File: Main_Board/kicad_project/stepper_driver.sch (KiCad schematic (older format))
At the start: 13 parts

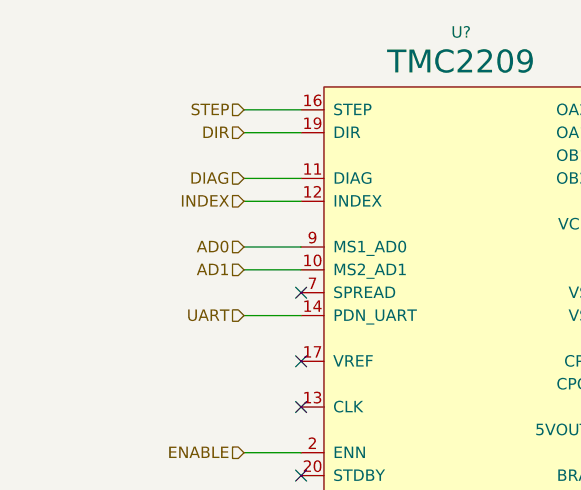
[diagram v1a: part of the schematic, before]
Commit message: add readmes, add MCU to main board, update footprints on interface board
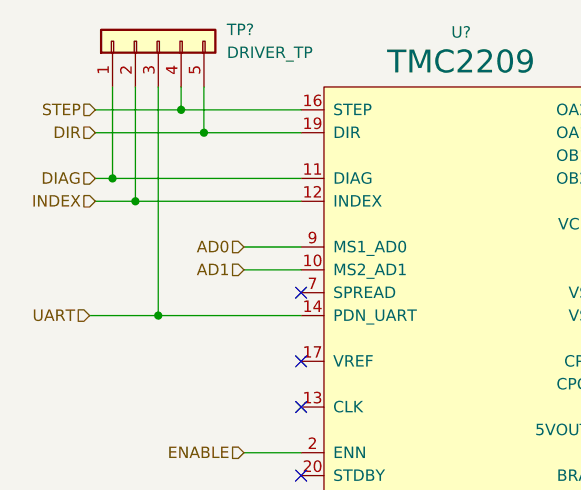
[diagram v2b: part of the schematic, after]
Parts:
- added TP?: DRIVER_TP, Connector_PinHeader_2.54mm:PinHeader_1x05_P2.54mm_Vertical, symbol Connector_Generic:Conn_01x05
- J?: footprint Connector_PinHeader_2.54mm:PinHeader_1x04_P2.54mm_Vertical -> Connector_PinHeader_2.54mm:PinHeader_1x04_P2.54mm_Horizontal
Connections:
- net DIAG: now also TP?.1 (Pin_1)
- net DIR: now also TP?.5 (Pin_5)
- net INDEX: now also TP?.2 (Pin_2)
- net STEP: now also TP?.4 (Pin_4)
- net UART: now also TP?.3 (Pin_3)
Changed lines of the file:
@@
 EESchema Schematic File Version 4
-LIBS:main_board-cache
-EELAYER 29 0
+EELAYER 30 0
 EELAYER END
 $Descr A4 11693 8268
 encoding utf-8
-Sheet 2 6
+Sheet 2 7
 Title ""
 Date ""
@@
 Text HLabel 4100 2950 0    50   Input ~ 0
 AD1
-Text HLabel 4100 3150 0    50   Input ~ 0
+Text HLabel 3425 3150 0    50   Input ~ 0
 UART
-Text HLabel 4100 2650 0    50   Input ~ 0
+Text HLabel 3450 2650 0    50   Input ~ 0
 INDEX
-Text HLabel 4100 2550 0    50   Input ~ 0
+Text HLabel 3450 2550 0    50   Input ~ 0
 DIAG
-Text HLabel 4100 2350 0    50   Input ~ 0
+Text HLabel 3450 2350 0    50   Input ~ 0
 DIR
-Text HLabel 4100 2250 0    50   Input ~ 0
+Text HLabel 3450 2250 0    50   Input ~ 0
 STEP
 Wire Wire Line
-	4350 2250 4100 2250
-Wire Wire Line
-	4100 2350 4350 2350
-Wire Wire Line
-	4350 2550 4100 2550
-Wire Wire Line
-	4100 2650 4350 2650
-Wire Wire Line
 	4350 2850 4100 2850
 Wire Wire Line
 	4100 2950 4350 2950
-Wire Wire Line
-	4350 3150 4100 3150
 Wire Wire Line
 	4350 3750 4100 3750
@@
 F 0 "J?" H 6405 2342 50  0000 L CNN
 F 1 "MOTOR" H 6405 2251 50  0000 L CNN
-F 2 "Connector_PinHeader_2.54mm:PinHeader_1x04_P2.54mm_Vertical" H 6325 2350 50  0001 C CNN
+F 2 "Connector_PinHeader_2.54mm:PinHeader_1x04_P2.54mm_Horizontal" H 6325 2350 50  0001 C CNN
 F 3 "~" H 6325 2350 50  0001 C CNN
 	1    6325 2350
@@
 Wire Wire Line
 	7550 3050 7600 3050
+$Comp
+L Connector_Generic:Conn_01x05 TP?
+U 1 1 5F51F4C4
+P 3725 1950
+F 0 "TP?" V 3775 1650 50  0000 R CNN
+F 1 "DRIVER_TP" V 3675 1650 50  0000 R CNN
+F 2 "Connector_PinHeader_2.54mm:PinHeader_1x05_P2.54mm_Vertical" H 3725 1950 50  0001 C CNN
+F 3 "~" H 3725 1950 50  0001 C CNN
+	1    3725 1950
+	0    -1   -1   0
+$EndComp
+Wire Wire Line
+	3450 2350 3925 2350
+Wire Wire Line
+	3450 2250 3825 2250
+Wire Wire Line
+	3450 2550 3525 2550
+Wire Wire Line
+	3450 2650 3625 2650
+Wire Wire Line
+	3425 3150 3725 3150
+Wire Wire Line
+	3525 2150 3525 2550
+Connection ~ 3525 2550
+Wire Wire Line
+	3525 2550 4350 2550
+Wire Wire Line
+	3625 2150 3625 2650
+Connection ~ 3625 2650
+Wire Wire Line
+	3625 2650 4350 2650
+Wire Wire Line
+	3725 2150 3725 3150
+Connection ~ 3725 3150
+Wire Wire Line
+	3725 3150 4350 3150
+Wire Wire Line
+	3825 2150 3825 2250
+Connection ~ 3825 2250
+Wire Wire Line
+	3825 2250 4350 2250
+Wire Wire Line
+	3925 2150 3925 2350
+Connection ~ 3925 2350
+Wire Wire Line
+	3925 2350 4350 2350
 $EndSCHEMATC

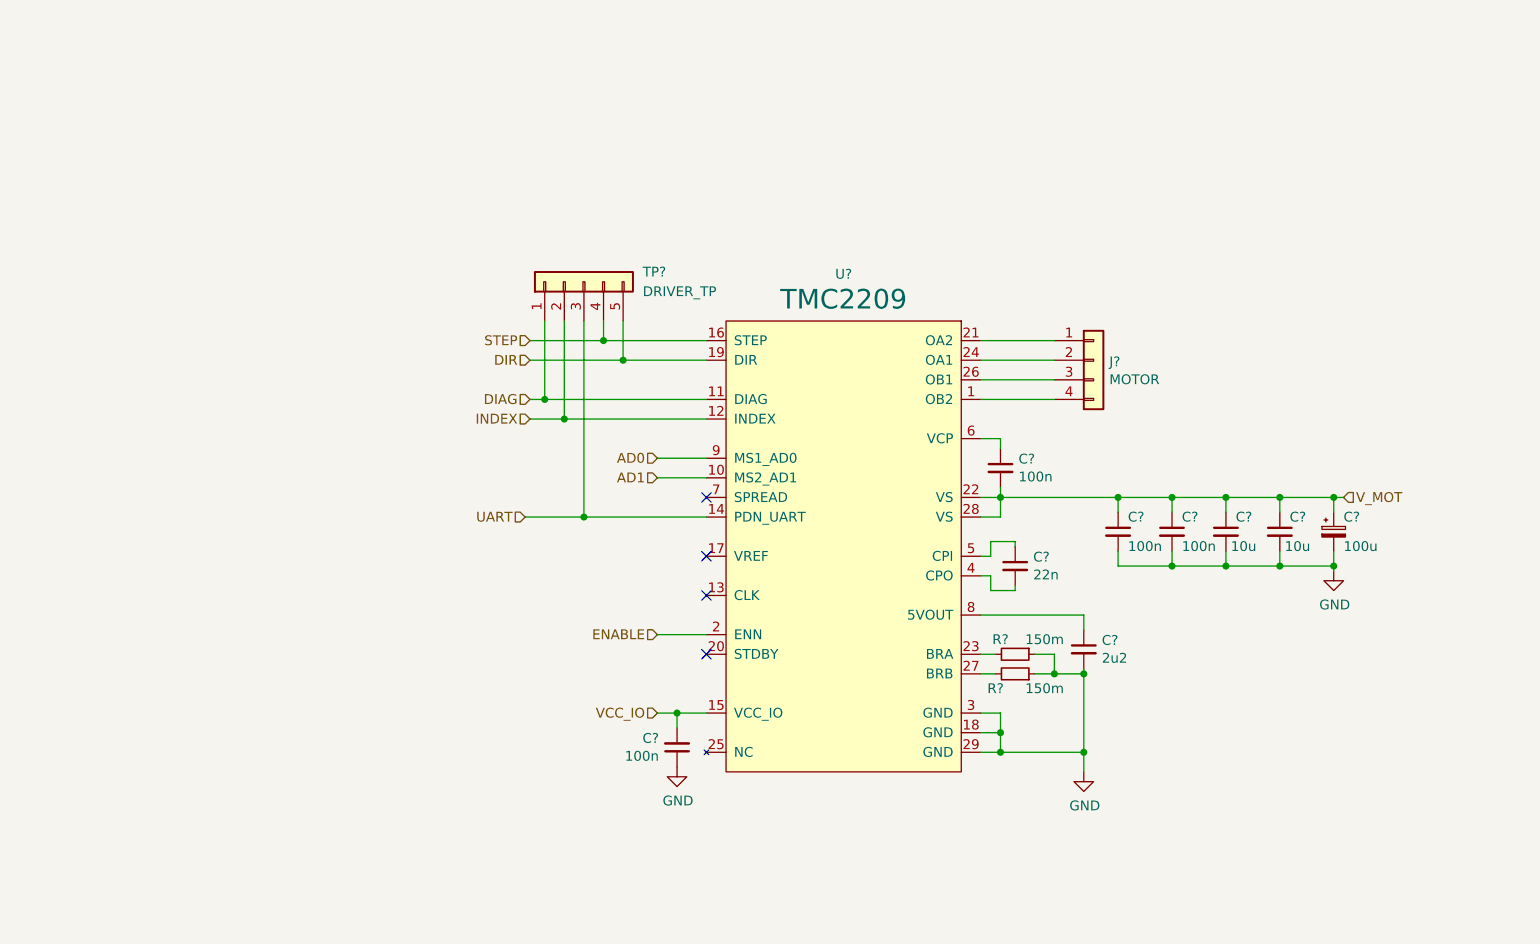
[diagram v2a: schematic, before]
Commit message: add input/output schematic, add documentation
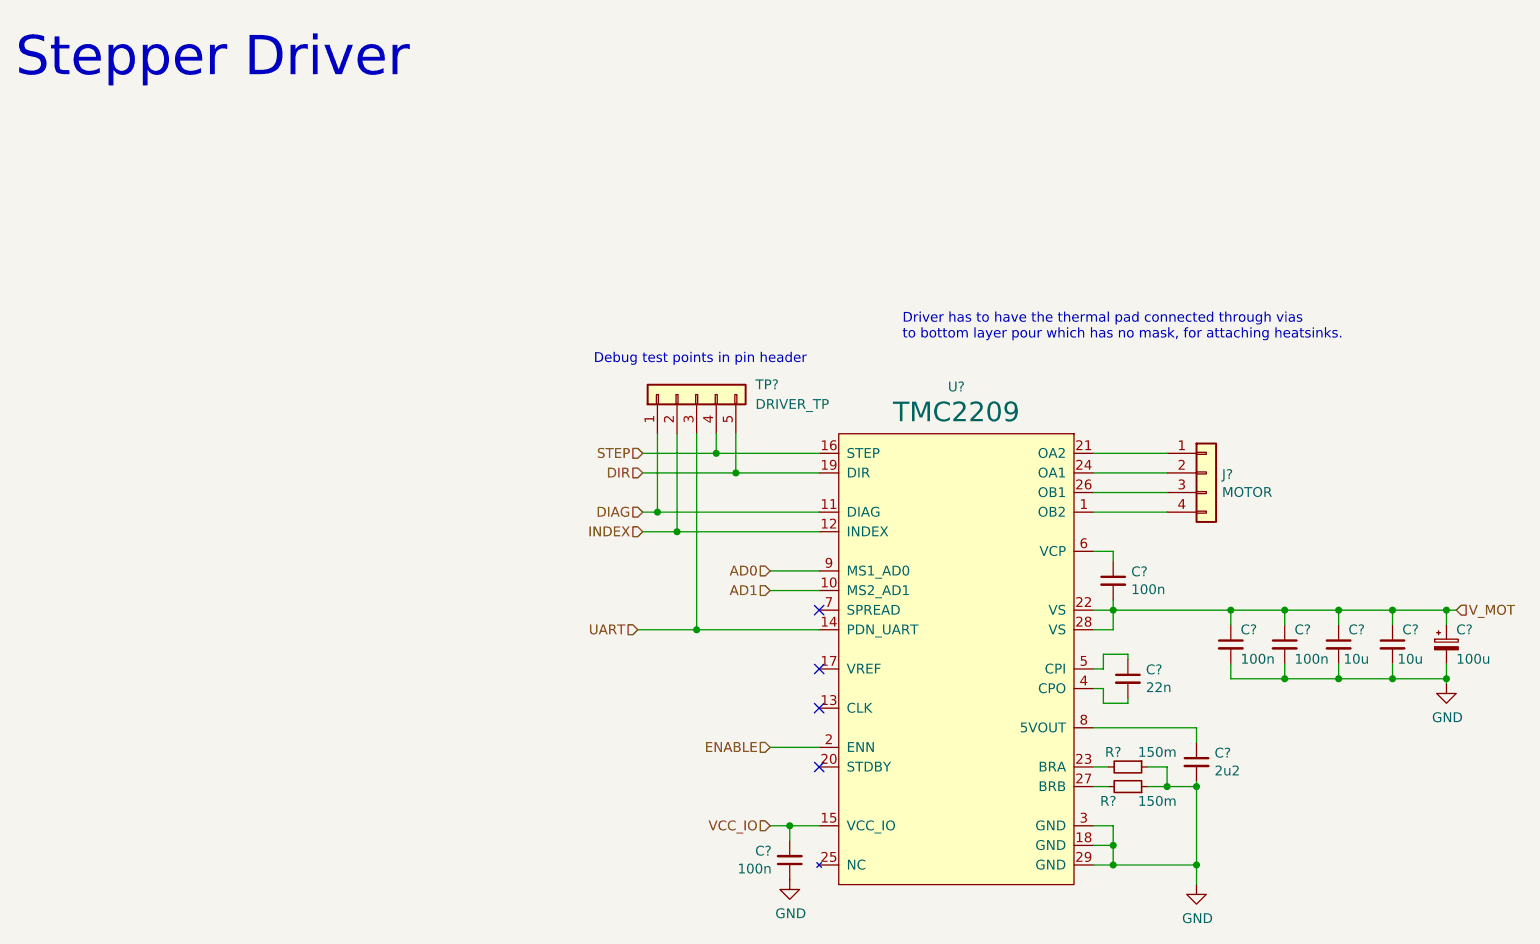
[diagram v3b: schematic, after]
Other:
- note added: "Debug test points in pin header"
- note added: "Driver has to have the thermal pad connected through vias\nto bottom layer pour which has no mask, for attaching heatsinks."
- note added: "Stepper Driver"
- moved on the sheet: C?, J?, R?, TP?, U?

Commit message: progress?
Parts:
- gave numbers to parts that had none: 14

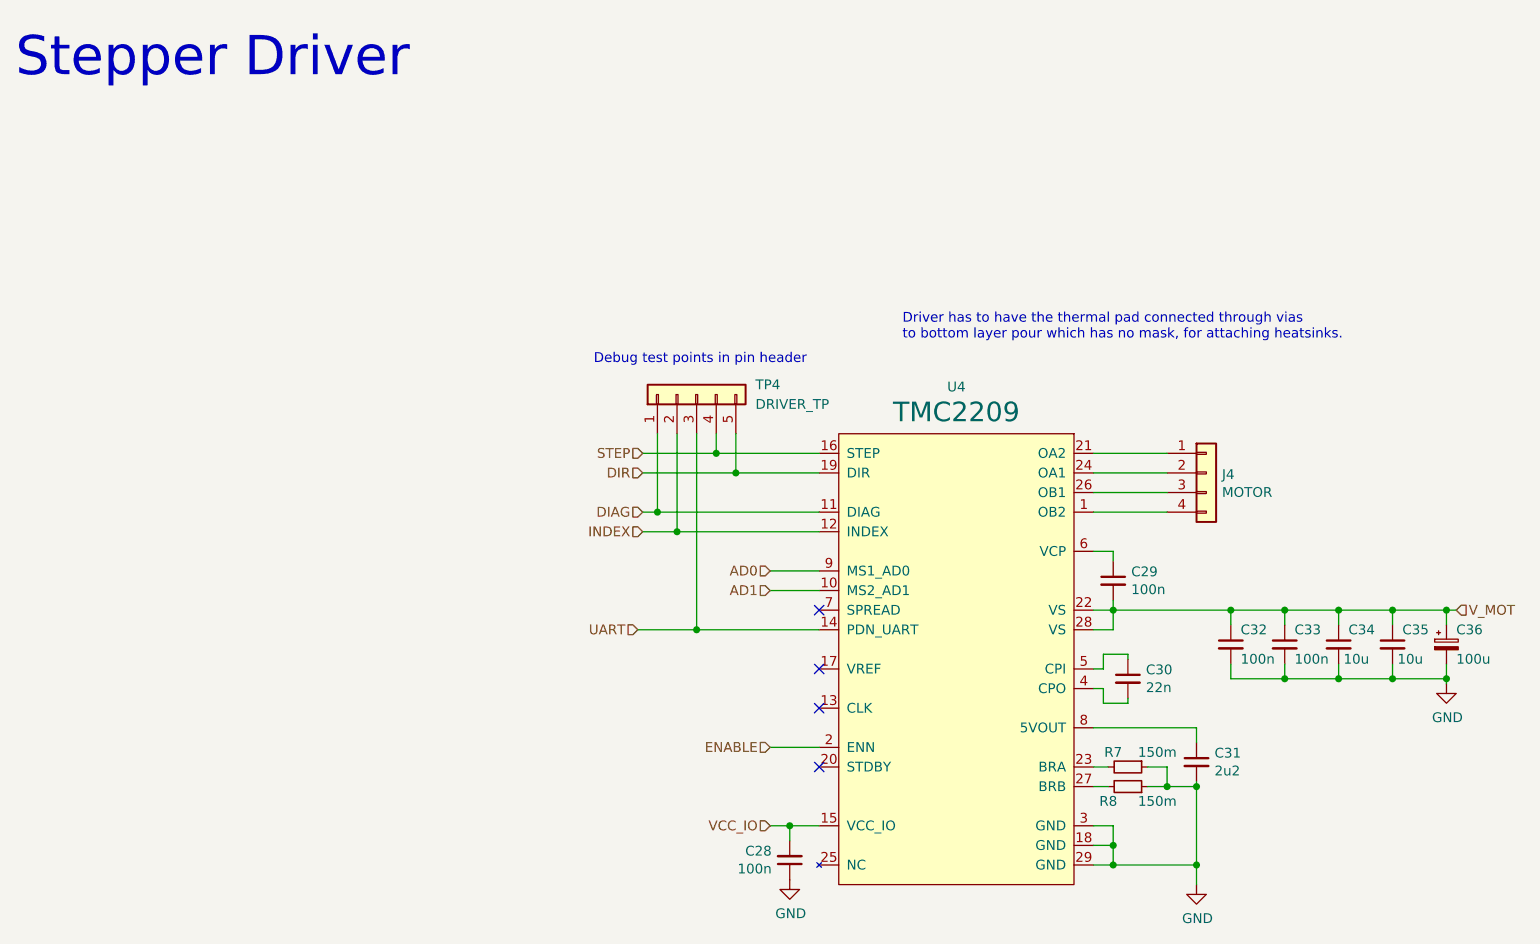
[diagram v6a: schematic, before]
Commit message: progress on MCU pinout
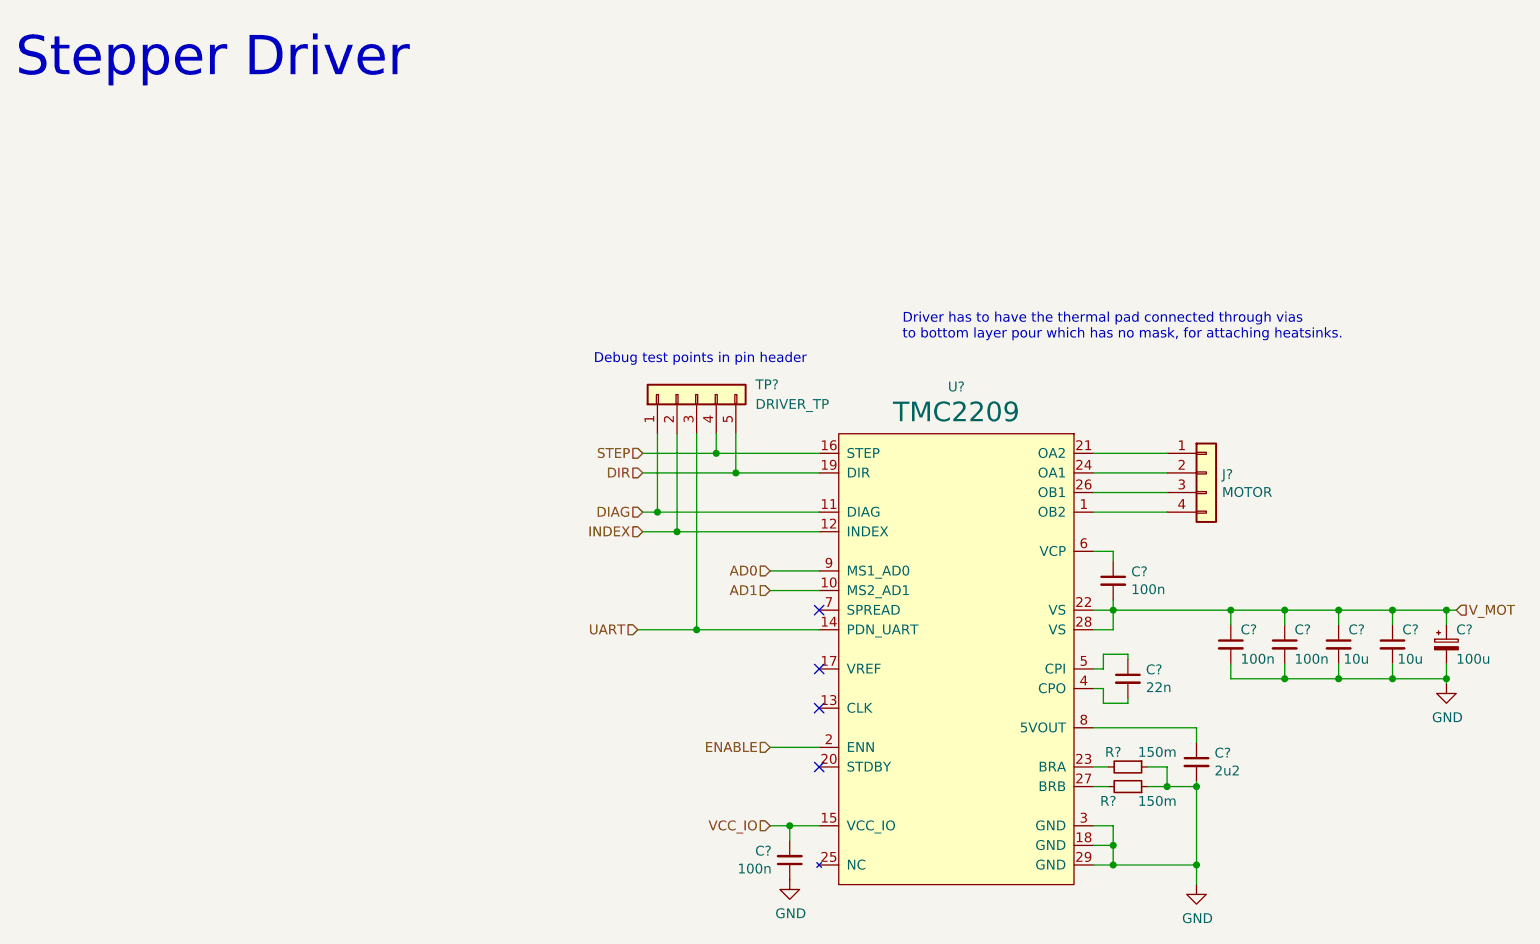
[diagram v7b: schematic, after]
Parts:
- renumbered C1 to C?, C2 to C?, C4 to C?, C3 to C?, C5 to C?, C6 to C?, C9 to C?, C7 to C?, C8 to C?, J1 to J?, R1 to R?, R2 to R?, TP1 to TP?, U1 to U?
